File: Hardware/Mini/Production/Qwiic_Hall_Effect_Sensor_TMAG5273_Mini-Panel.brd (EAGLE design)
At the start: 175 x 93 mm, 1302 parts, among them J1 Vertical Qwiic Connector, J10 Vertical Qwiic Connector, J100 Vertical Qwiic Connector, J101 Vertical Qwiic Connector, J103 Vertical Qwiic Connector, J104 Vertical Qwiic Connector, J106 Vertical Qwiic Connector, J107 Vertical Qwiic Connector, J11 Vertical Qwiic Connector, J13 Vertical Qwiic Connector, J14 Vertical Qwiic Connector, J16 Vertical Qwiic Connector, J17 Vertical Qwiic Connector, J19 Vertical Qwiic Connector, J2 Vertical Qwiic Connector, J20 Vertical Qwiic Connector, J22 Vertical Qwiic Connector, J23 Vertical Qwiic Connector, J25 Vertical Qwiic Connector, J26 Vertical Qwiic Connector, J28 Vertical Qwiic Connector, J29 Vertical Qwiic Connector, J31 Vertical Qwiic Connector, J32 Vertical Qwiic Connector, J34 Vertical Qwiic Connector, J35 Vertical Qwiic Connector, J37 Vertical Qwiic Connector, J38 Vertical Qwiic Connector, J4 Vertical Qwiic Connector, J40 Vertical Qwiic Connector, J41 Vertical Qwiic Connector, J43 Vertical Qwiic Connector, J44 Vertical Qwiic Connector, J46 Vertical Qwiic Connector, J47 Vertical Qwiic Connector, J49 Vertical Qwiic Connector, J5 Vertical Qwiic Connector, J50 Vertical Qwiic Connector, J52 Vertical Qwiic Connector, J53 Vertical Qwiic Connector, J55 Vertical Qwiic Connector, J56 Vertical Qwiic Connector, J58 Vertical Qwiic Connector, J59 Vertical Qwiic Connector, J61 Vertical Qwiic Connector, J62 Vertical Qwiic Connector, J64 Vertical Qwiic Connector, J65 Vertical Qwiic Connector, J67 Vertical Qwiic Connector, J68 Vertical Qwiic Connector, J7 Vertical Qwiic Connector, J70 Vertical Qwiic Connector, J71 Vertical Qwiic Connector, J73 Vertical Qwiic Connector, J74 Vertical Qwiic Connector, J76 Vertical Qwiic Connector, J77 Vertical Qwiic Connector, J79 Vertical Qwiic Connector, J8 Vertical Qwiic Connector, J80 Vertical Qwiic Connector, J82 Vertical Qwiic Connector, J83 Vertical Qwiic Connector, J85 Vertical Qwiic Connector, J86 Vertical Qwiic Connector, J88 Vertical Qwiic Connector, J89 Vertical Qwiic Connector, J91 Vertical Qwiic Connector, J92 Vertical Qwiic Connector, J94 Vertical Qwiic Connector, J95 Vertical Qwiic Connector, J97 Vertical Qwiic Connector, J98 Vertical Qwiic Connector, Q1 20V/4.2A/52mΩ/1.4W, Q10 20V/4.2A/52mΩ/1.4W, Q11 20V/4.2A/52mΩ/1.4W, Q12 20V/4.2A/52mΩ/1.4W, Q13 20V/4.2A/52mΩ/1.4W, Q14 20V/4.2A/52mΩ/1.4W, Q15 20V/4.2A/52mΩ/1.4W, Q16 20V/4.2A/52mΩ/1.4W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

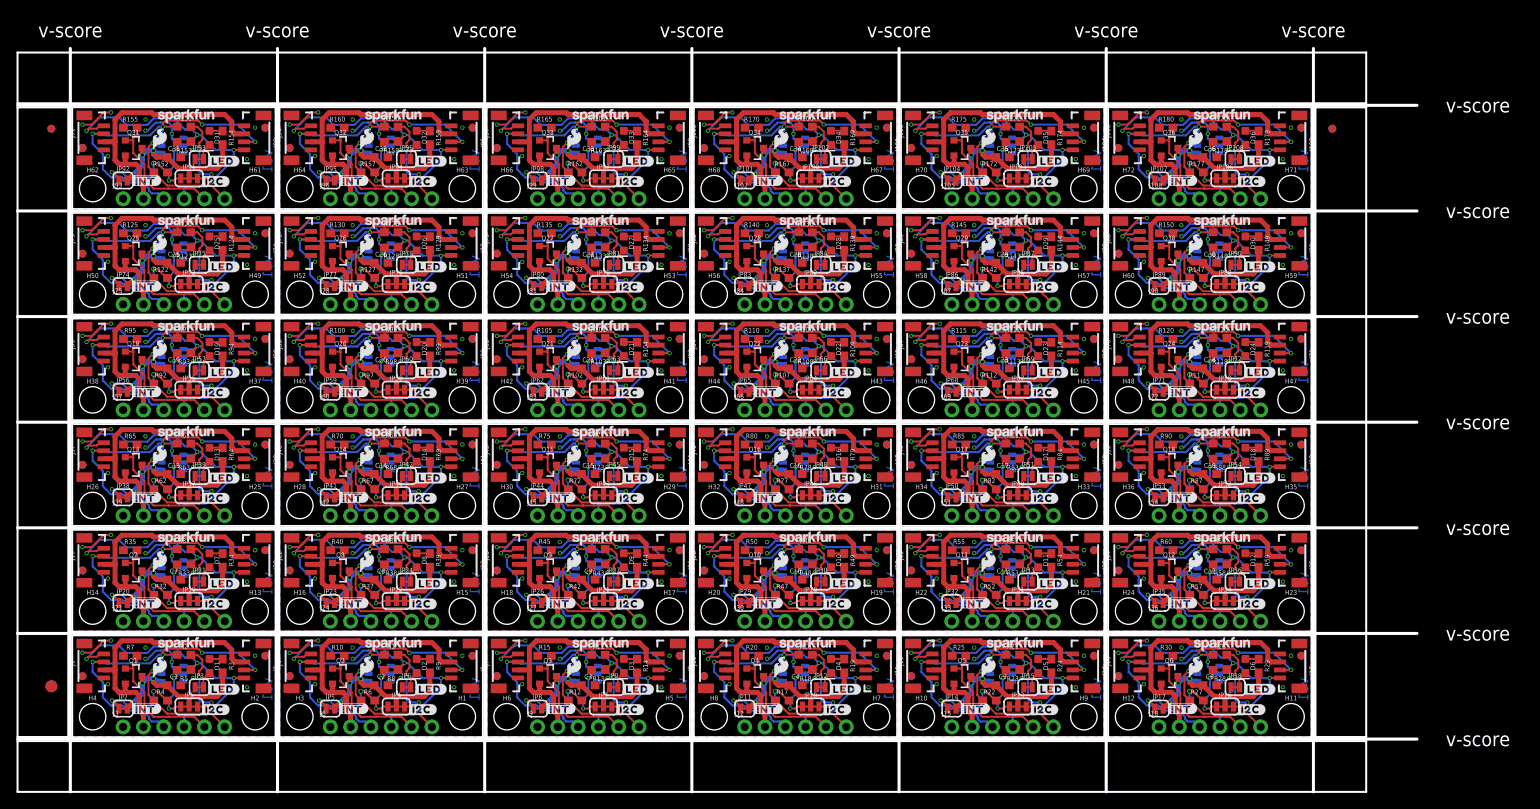
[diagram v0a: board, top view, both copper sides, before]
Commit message: Files for ordering
Re-added the correct panel files for the project along with ordering instructions. Made final adjustments from design review and board is ready for order!
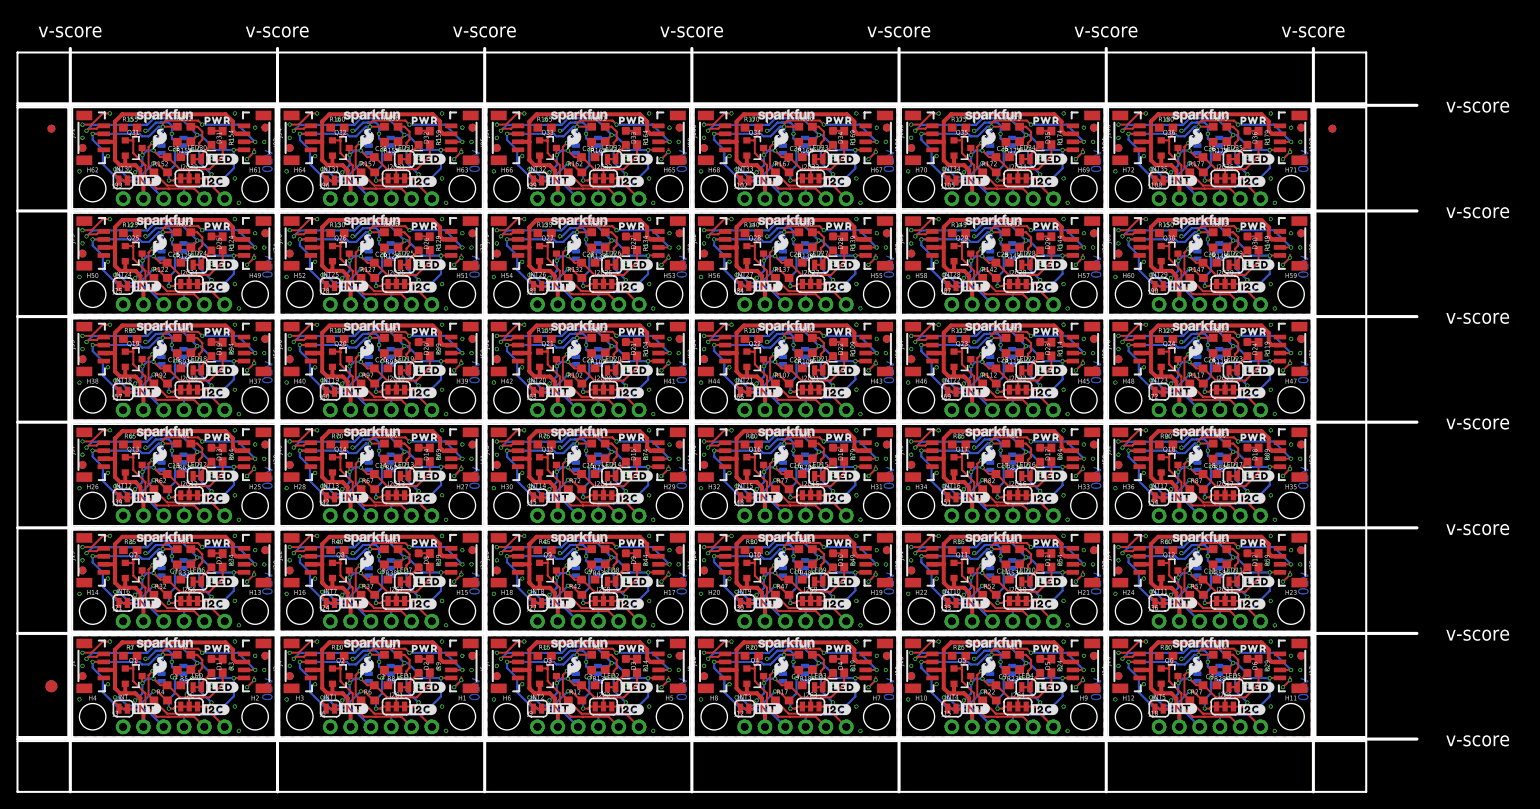
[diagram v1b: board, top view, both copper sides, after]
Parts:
- removed JP102, JP105, JP108, JP12, JP15, JP18, JP21, JP24, JP27, JP3, JP30, JP33, JP36, JP39, JP42, JP45, JP48, JP51, JP54, JP57, JP6, JP60, JP63, JP66, JP69, JP72, JP75, JP78, JP81, JP84, JP87, JP9, JP90, JP93, JP96, JP99: JUMPER-SMT_2_NC_TRACE_SILK, SparkFun-Jumpers:SMT-JUMPER_2_NC_TRACE_SILK
- added LED, LED1, LED10, LED11, LED12, LED13, LED14, LED15, LED16, LED17, LED18, LED19, LED2, LED20, LED21, LED22, LED23, LED24, LED25, LED26, LED27, LED28, LED29, LED3, LED30, LED31, LED32, LED33, LED34, LED35, LED4, LED5, LED6, LED7, LED8, LED9: JUMPER-SMT_2_NC_TRACE_SILK, SparkFun-Jumpers:SMT-JUMPER_2_NC_TRACE_SILK
- added U$361, U$372, U$383, U$394: (no value), output:#INT#5285
- added U$362, U$373, U$384, U$395: (no value), output:#INT#5287
- added U$363, U$374, U$385, U$396: (no value), output:#DISABLE#5291
- added U$364, U$375, U$386: (no value), output:#SCL#38
- added U$365, U$376, U$387: (no value), output:#SDA#37
- added U$366, U$377, U$388: (no value), output:#3V3#37
- added U$367, U$378, U$389: (no value), output:#GND#36
- added U$368, U$379, U$390: (no value), output:TMAG5273_HALL#EFFECT_SENSOR0
- added U$369, U$380, U$391: (no value), output:#I2C#5276
- added U$370, U$381, U$392: (no value), output:#LED#5275
- added U$371, U$382, U$393: (no value), output:PWR5282
- U$1, U$151, U$261, U$41: device output:#SCL#38 -> output:PWR5282
- U$100, U$210, U$320: device output:#DISABLE#5279 -> output:#SCL#38
- U$101, U$211, U$321: device output:#SCL#38 -> output:#SDA#37
- U$102, U$212, U$322: device output:#SDA#37 -> output:#3V3#37
- U$103, U$213, U$323: device output:#3V3#37 -> output:#GND#36
- U$104, U$214, U$324: device output:#GND#36 -> output:TMAG5273_HALL#EFFECT_SENSOR0
- U$105, U$215, U$325: device output:TMAG5273_HALL#EFFECT_SENSOR0 -> output:#I2C#5276
- U$106, U$216, U$326: device output:##INT#5275 -> output:#LED#5275
- U$107, U$217, U$327: device output:#I2C#5276 -> output:PWR5282
- U$108, U$218, U$328: device output:#LED#5275 -> output:#INT#5285
- U$109, U$219, U$329: device output:##INT#5276 -> output:#INT#5287
- U$11, U$122, U$232, U$342: device output:#SDA#37 -> output:#SCL#38
- U$110, U$220, U$330: device output:#DISABLE#5279 -> output:#DISABLE#5291
- U$116, U$226, U$336: device output:##INT#5275 -> output:#I2C#5276
- U$117, U$227, U$337: device output:#I2C#5276 -> output:#LED#5275
- U$118, U$228, U$338: device output:#LED#5275 -> output:PWR5282
- U$119, U$229, U$339: device output:##INT#5276 -> output:#INT#5285
- U$12, U$153, U$263, U$43: device output:#3V3#37 -> output:#INT#5287
- U$120, U$230, U$340: device output:#DISABLE#5279 -> output:#INT#5287
- U$121, U$231, U$341: device output:#SCL#38 -> output:#DISABLE#5291
- U$123, U$233, U$343: device output:#3V3#37 -> output:#SDA#37
- U$124, U$234, U$344: device output:#GND#36 -> output:#3V3#37
- U$125, U$235, U$345: device output:TMAG5273_HALL#EFFECT_SENSOR0 -> output:#GND#36
- U$126, U$16, U$236, U$346: device output:##INT#5275 -> output:TMAG5273_HALL#EFFECT_SENSOR0
- U$129, U$19, U$239, U$349: device output:##INT#5276 -> output:PWR5282
- U$13, U$134, U$24, U$244, U$354: device output:#GND#36 -> output:#SDA#37
- U$130, U$20, U$240, U$350, U$9: device output:#DISABLE#5279 -> output:#INT#5285
- U$131, U$21, U$241, U$351: device output:#SCL#38 -> output:#INT#5287
- U$132, U$22, U$242, U$352: device output:#SDA#37 -> output:#DISABLE#5291
- U$133, U$23, U$243, U$353: device output:#3V3#37 -> output:#SCL#38
- U$135, U$14, U$245, U$25, U$355: device output:TMAG5273_HALL#EFFECT_SENSOR0 -> output:#3V3#37
- U$136, U$246, U$26, U$356: device output:##INT#5275 -> output:#GND#36
- U$137, U$247, U$27, U$357: device output:#I2C#5276 -> output:TMAG5273_HALL#EFFECT_SENSOR0
- U$138, U$248, U$28, U$358: device output:#LED#5275 -> output:#I2C#5276
- U$139, U$249, U$29, U$359: device output:##INT#5276 -> output:#LED#5275
- U$140, U$250, U$30, U$360: device output:#DISABLE#5279 -> output:PWR5282
- U$141, U$251, U$31: device output:#SCL#38 -> output:#INT#5285
- U$142, U$252, U$32: device output:#SDA#37 -> output:#INT#5287
- U$143, U$253, U$33: device output:#3V3#37 -> output:#DISABLE#5291
- U$144, U$254, U$34: device output:#GND#36 -> output:#SCL#38
- U$145, U$255, U$35: device output:TMAG5273_HALL#EFFECT_SENSOR0 -> output:#SDA#37
- U$146, U$256, U$36: device output:##INT#5275 -> output:#3V3#37
- U$147, U$257, U$37: device output:#I2C#5276 -> output:#GND#36
- U$148, U$258, U$38: device output:#LED#5275 -> output:TMAG5273_HALL#EFFECT_SENSOR0
- U$149, U$259, U$39: device output:##INT#5276 -> output:#I2C#5276
- U$15, U$169, U$279, U$59: device output:##INT#5276 -> output:#GND#36
- U$150, U$260, U$40: device output:#DISABLE#5279 -> output:#LED#5275
- U$152, U$262, U$42: device output:#SDA#37 -> output:#INT#5285
- U$154, U$264, U$44: device output:#GND#36 -> output:#DISABLE#5291
- U$155, U$265, U$45: device output:TMAG5273_HALL#EFFECT_SENSOR0 -> output:#SCL#38
- U$156, U$266, U$46: device output:##INT#5275 -> output:#SDA#37
- U$157, U$267, U$47: device output:#I2C#5276 -> output:#3V3#37
- U$158, U$268, U$48: device output:#LED#5275 -> output:#GND#36
- U$159, U$269, U$49: device output:##INT#5276 -> output:TMAG5273_HALL#EFFECT_SENSOR0
- U$160, U$270, U$50: device output:#DISABLE#5279 -> output:#I2C#5276
- U$161, U$271, U$51: device output:#SCL#38 -> output:#LED#5275
- U$162, U$272, U$52: device output:#SDA#37 -> output:PWR5282
- U$163, U$273, U$53: device output:#3V3#37 -> output:#INT#5285
- U$164, U$274, U$54: device output:#GND#36 -> output:#INT#5287
- U$165, U$275, U$55: device output:TMAG5273_HALL#EFFECT_SENSOR0 -> output:#DISABLE#5291
- U$166, U$276, U$56: device output:##INT#5275 -> output:#SCL#38
- U$167, U$277, U$57: device output:#I2C#5276 -> output:#SDA#37
- U$168, U$278, U$58: device output:#LED#5275 -> output:#3V3#37
- U$170, U$280, U$60: device output:#DISABLE#5279 -> output:TMAG5273_HALL#EFFECT_SENSOR0
- U$171, U$281, U$61: device output:#SCL#38 -> output:#I2C#5276
- U$172, U$282, U$62: device output:#SDA#37 -> output:#LED#5275
- U$173, U$283, U$63: device output:#3V3#37 -> output:PWR5282
- U$174, U$284, U$64: device output:#GND#36 -> output:#INT#5285
- U$175, U$285, U$65: device output:TMAG5273_HALL#EFFECT_SENSOR0 -> output:#INT#5287
- U$176, U$286, U$66, U$7: device output:##INT#5275 -> output:#DISABLE#5291
- U$177, U$287, U$67: device output:#I2C#5276 -> output:#SCL#38
- U$178, U$288, U$68: device output:#LED#5275 -> output:#SDA#37
- U$179, U$289, U$69: device output:##INT#5276 -> output:#3V3#37
- U$180, U$290, U$70: device output:#DISABLE#5279 -> output:#GND#36
- U$181, U$291, U$71: device output:#SCL#38 -> output:TMAG5273_HALL#EFFECT_SENSOR0
- U$182, U$292, U$72: device output:#SDA#37 -> output:#I2C#5276
- U$183, U$293, U$73: device output:#3V3#37 -> output:#LED#5275
- U$184, U$294, U$74: device output:#GND#36 -> output:PWR5282
- U$185, U$295, U$75: device output:TMAG5273_HALL#EFFECT_SENSOR0 -> output:#INT#5285
- U$186, U$296, U$76: device output:##INT#5275 -> output:#INT#5287
- U$187, U$297, U$77: device output:#I2C#5276 -> output:#DISABLE#5291
- U$188, U$298, U$78: device output:#LED#5275 -> output:#SCL#38
- U$189, U$299, U$79: device output:##INT#5276 -> output:#SDA#37
- U$190, U$300, U$80: device output:#DISABLE#5279 -> output:#3V3#37
- U$191, U$301, U$81: device output:#SCL#38 -> output:#GND#36
- U$192, U$302, U$82: device output:#SDA#37 -> output:TMAG5273_HALL#EFFECT_SENSOR0
- U$193, U$303, U$83: device output:#3V3#37 -> output:#I2C#5276
- U$194, U$304, U$84: device output:#GND#36 -> output:#LED#5275
- U$195, U$305, U$85: device output:TMAG5273_HALL#EFFECT_SENSOR0 -> output:PWR5282
- U$196, U$306, U$86: device output:##INT#5275 -> output:#INT#5285
- U$197, U$307, U$87: device output:#I2C#5276 -> output:#INT#5287
- U$198, U$308, U$88: device output:#LED#5275 -> output:#DISABLE#5291
- U$199, U$309, U$89: device output:##INT#5276 -> output:#SCL#38
- U$200, U$310, U$90: device output:#DISABLE#5279 -> output:#SDA#37
- U$201, U$311, U$91: device output:#SCL#38 -> output:#3V3#37
- U$202, U$312, U$92: device output:#SDA#37 -> output:#GND#36
- U$203, U$313, U$93: device output:#3V3#37 -> output:TMAG5273_HALL#EFFECT_SENSOR0
- U$204, U$314, U$94: device output:#GND#36 -> output:#I2C#5276
- U$205, U$315, U$95: device output:TMAG5273_HALL#EFFECT_SENSOR0 -> output:#LED#5275
- U$206, U$316, U$96: device output:##INT#5275 -> output:PWR5282
- U$207, U$317, U$97: device output:#I2C#5276 -> output:#INT#5285
- U$208, U$318, U$98: device output:#LED#5275 -> output:#INT#5287
- U$209, U$319, U$99: device output:##INT#5276 -> output:#DISABLE#5291
- moved U$64 142.9 mm to (148.6, 3.68)
- moved U$63 138.9 mm to (147.7, 11.0), flipped to the top, turned to 0 degrees
- moved U$66 137.4 mm to (146.1, 5.46), flipped to the bottom, turned to 270 degrees
- moved U$62 137.2 mm to (148.2, 6.22), flipped to the top, turned to 0 degrees
- moved U$61 134.0 mm to (147.3, 3.43), flipped to the top, turned to 0 degrees
- moved U$126 132.9 mm to (142.0, 24.6), flipped to the bottom
- moved U$130 132.9 mm to (148.6, 16.9)
- moved U$122 132.8 mm to (143.5, 17.0)
- moved U$124 132.7 mm to (138.4, 17.1)
- moved U$123 132.7 mm to (141.0, 17.1)
- moved U$127 130.2 mm to (147.3, 16.6)
- moved U$128 130.1 mm to (148.2, 19.4)
- moved U$129 128.8 mm to (147.7, 24.3), flipped to the top, turned to 0 degrees
- moved U$65 128.0 mm to (138.7, 3.56), flipped to the top
- moved U$188 125.7 mm to (143.5, 30.2), flipped to the bottom, turned to 270 degrees
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- renumbered JP1 to I2C, JP10 to I2C3, JP100 to I2C33, JP101 to INT33, JP103 to I2C34, JP104 to INT34, JP106 to I2C35, JP107 to INT35, JP11 to INT3, JP13 to I2C4, JP14 to INT4, JP16 to I2C5, JP17 to INT5, JP19 to I2C6, JP2 to INT, JP20 to INT6, JP22 to I2C7, JP23 to INT7, JP25 to I2C8, JP26 to INT8, JP28 to I2C9, JP29 to INT9, JP31 to I2C10, JP32 to INT10, JP34 to I2C11, JP35 to INT11, JP37 to I2C12, JP38 to INT12, JP4 to I2C1, JP40 to I2C13, JP41 to INT13, JP43 to I2C14, JP44 to INT14, JP46 to I2C15, JP47 to INT15, JP49 to I2C16, JP5 to INT1, JP50 to INT16, JP52 to I2C17, JP53 to INT17, JP55 to I2C18, JP56 to INT18, JP58 to I2C19, JP59 to INT19, JP61 to I2C20, JP62 to INT20, JP64 to I2C21, JP65 to INT21, JP67 to I2C22, JP68 to INT22, JP7 to I2C2, JP70 to I2C23, JP71 to INT23, JP73 to I2C24, JP74 to INT24, JP76 to I2C25, JP77 to INT25, JP79 to I2C26, JP8 to INT2, JP80 to INT26, JP82 to I2C27, JP83 to INT27, JP85 to I2C28, JP86 to INT28, JP88 to I2C29, JP89 to INT29, JP91 to I2C30, JP92 to INT30, JP94 to I2C31, JP95 to INT31, JP97 to I2C32, JP98 to INT32
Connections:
- net GND: now also LED.1; no longer JP3.1
- net GND1: now also LED1.1; no longer JP6.1
- net GND10: now also LED10.1; no longer JP33.1
- net GND11: now also LED11.1; no longer JP36.1
- net GND12: now also LED12.1; no longer JP39.1
- net GND13: now also LED13.1; no longer JP42.1
- net GND14: now also LED14.1; no longer JP45.1
- net GND15: now also LED15.1; no longer JP48.1
- net GND16: now also LED16.1; no longer JP51.1
- net GND17: now also LED17.1; no longer JP54.1
- net GND18: now also LED18.1; no longer JP57.1
- net GND19: now also LED19.1; no longer JP60.1
- net GND2: now also LED2.1; no longer JP9.1
- net GND20: now also LED20.1; no longer JP63.1
- net GND21: now also LED21.1; no longer JP66.1
- net GND22: now also LED22.1; no longer JP69.1
- net GND23: now also LED23.1; no longer JP72.1
- net GND24: now also LED24.1; no longer JP75.1
- net GND25: now also LED25.1; no longer JP78.1
- net GND26: now also LED26.1; no longer JP81.1
- net GND27: now also LED27.1; no longer JP84.1
- net GND28: now also LED28.1; no longer JP87.1
- net GND29: now also LED29.1; no longer JP90.1
- net GND3: now also LED3.1; no longer JP12.1
- net GND30: now also LED30.1; no longer JP93.1
- net GND31: now also LED31.1; no longer JP96.1
- net GND32: now also LED32.1; no longer JP99.1
- net GND33: now also LED33.1; no longer JP102.1
- net GND34: now also LED34.1; no longer JP105.1
- net GND35: now also LED35.1; no longer JP108.1
- net GND4: now also LED4.1; no longer JP15.1
- net GND5: now also LED5.1; no longer JP18.1
- net GND6: now also LED6.1; no longer JP21.1
- net GND7: now also LED7.1; no longer JP24.1
- net GND8: now also LED8.1; no longer JP27.1
- net GND9: now also LED9.1; no longer JP30.1
- net N$1: now also LED.2; no longer JP3.2
- net N$102: now also LED20.2; no longer JP63.2
- net N$107: now also LED21.2; no longer JP66.2
- net N$112: now also LED22.2; no longer JP69.2
- net N$117: now also LED23.2; no longer JP72.2
- net N$12: now also LED2.2; no longer JP9.2
- net N$122: now also LED24.2; no longer JP75.2
- net N$127: now also LED25.2; no longer JP78.2
- net N$132: now also LED26.2; no longer JP81.2
- net N$137: now also LED27.2; no longer JP84.2
- net N$142: now also LED28.2; no longer JP87.2
- net N$147: now also LED29.2; no longer JP90.2
- net N$152: now also LED30.2; no longer JP93.2
- net N$157: now also LED31.2; no longer JP96.2
- net N$162: now also LED32.2; no longer JP99.2
- net N$167: now also LED33.2; no longer JP102.2
- net N$17: now also LED3.2; no longer JP12.2
- net N$172: now also LED34.2; no longer JP105.2
- net N$177: now also LED35.2; no longer JP108.2
- net N$22: now also LED4.2; no longer JP15.2
- net N$27: now also LED5.2; no longer JP18.2
- net N$32: now also LED6.2; no longer JP21.2
- net N$37: now also LED7.2; no longer JP24.2
- net N$42: now also LED8.2; no longer JP27.2
- net N$47: now also LED9.2; no longer JP30.2
- net N$52: now also LED10.2; no longer JP33.2
- net N$57: now also LED11.2; no longer JP36.2
- net N$62: now also LED12.2; no longer JP39.2
- net N$67: now also LED13.2; no longer JP42.2
- net N$7: now also LED1.2; no longer JP6.2
- net N$72: now also LED14.2; no longer JP45.2
- net N$77: now also LED15.2; no longer JP48.2
- net N$82: now also LED16.2; no longer JP51.2
- net N$87: now also LED17.2; no longer JP54.2
- net N$92: now also LED18.2; no longer JP57.2
- net N$97: now also LED19.2; no longer JP60.2
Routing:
- net GND2: track 11.5 -> 13.0 mm, vias 9 -> 18
- net GND8: track 11.5 -> 13.0 mm, vias 9 -> 18
- net GND4: track 11.5 -> 13.0 mm, vias 9 -> 18
- net GND10: track 11.5 -> 13.0 mm, vias 9 -> 18
- net GND5: track 11.5 -> 13.0 mm, vias 9 -> 18
- net GND3: track 11.5 -> 13.0 mm, vias 9 -> 18
- net GND26: track 11.5 -> 13.0 mm, vias 9 -> 18
- net GND20: track 11.5 -> 13.0 mm, vias 9 -> 18
- net GND14: track 11.5 -> 13.0 mm, vias 9 -> 18
- net GND6: track 11.5 -> 13.0 mm, vias 9 -> 18
- net GND28: track 11.5 -> 13.0 mm, vias 9 -> 18
- net GND22: track 11.5 -> 13.0 mm, vias 9 -> 18
- net GND16: track 11.5 -> 13.0 mm, vias 9 -> 18
- net GND11: track 11.5 -> 13.0 mm, vias 9 -> 18
- net GND: track 11.5 -> 13.0 mm, vias 9 -> 18
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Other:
- board text added: "v10"
- board text removed: "v01"
